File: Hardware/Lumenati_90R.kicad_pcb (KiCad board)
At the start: 2 copper layers, 25.4 x 25.4 mm, 19 parts, among them J1 CONN_041X04_NO_SILK, J2 CONN_041X04_NO_SILK, U1 APA102, U2 APA102, U3 APA102

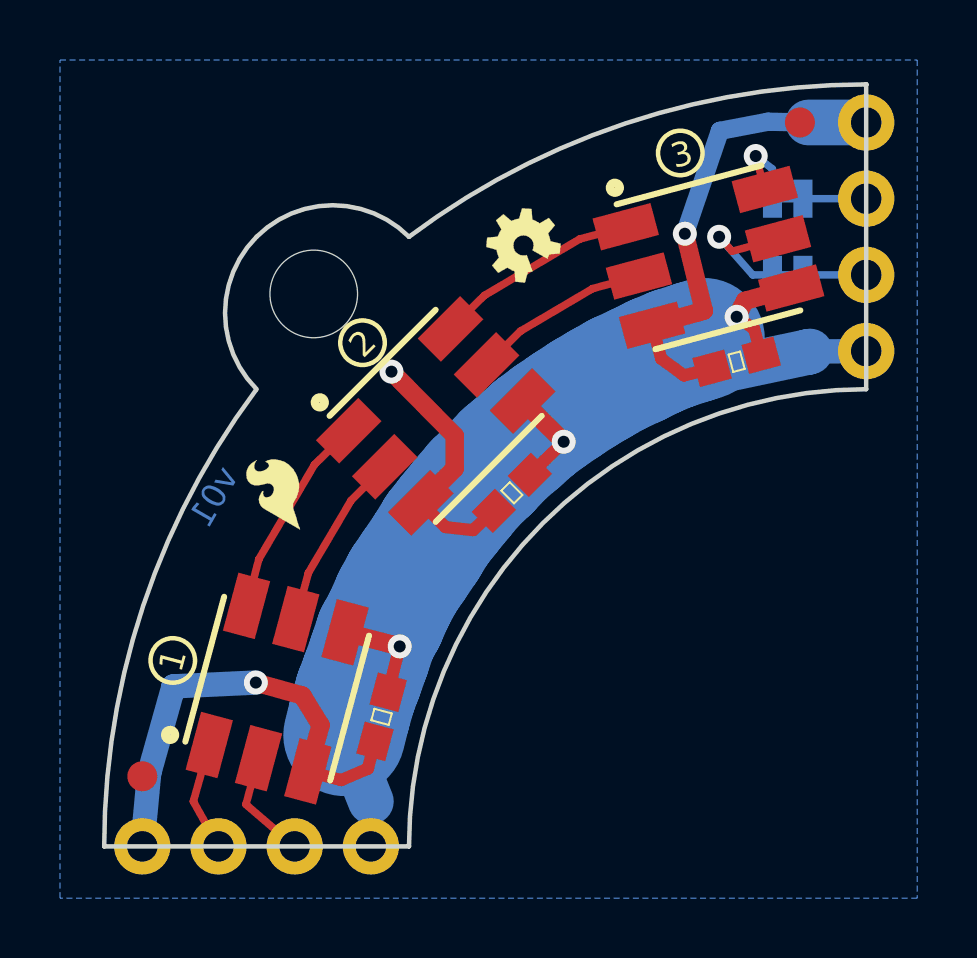
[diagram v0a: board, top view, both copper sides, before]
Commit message: Changed all the names to Lumenati, updated version to v10.
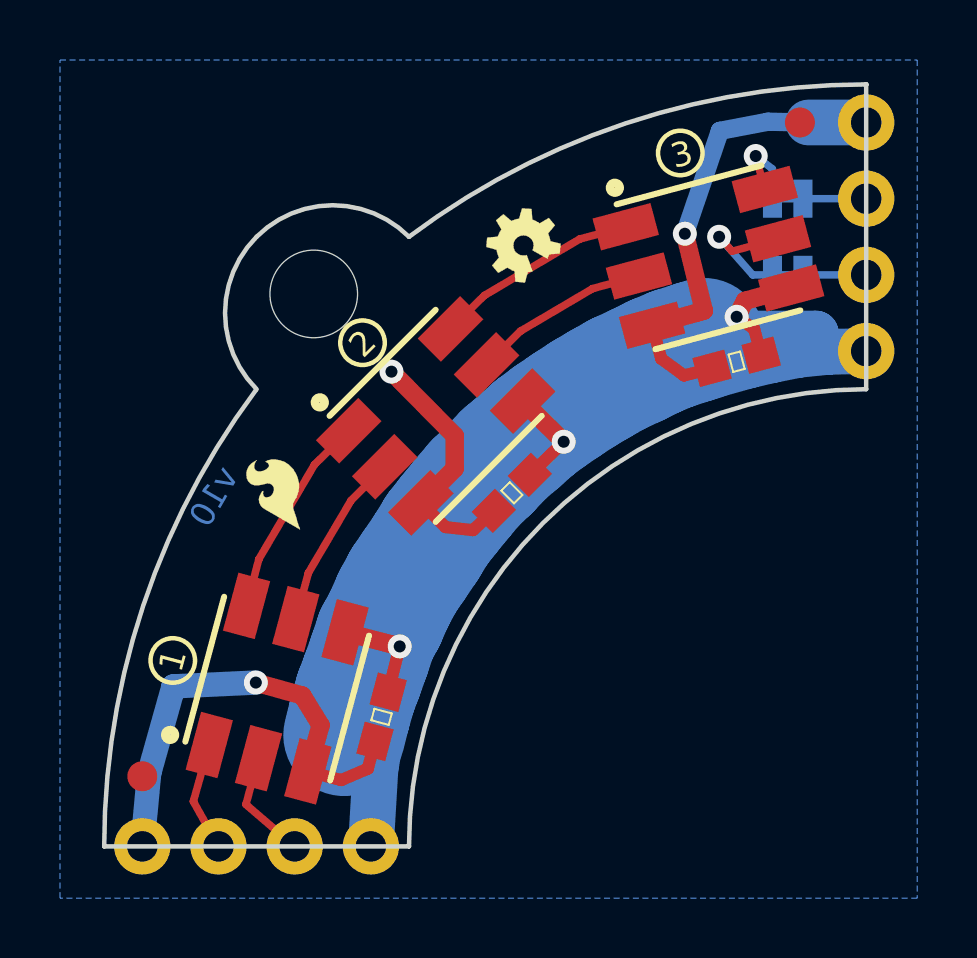
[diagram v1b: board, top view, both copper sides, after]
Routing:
- net +5V: track 45.1 -> 52.0 mm
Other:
- board text added: "Lumenati 90R"
- board text added: "v10"
- board text removed: "HiBeams 90R"
- board text removed: "v01"
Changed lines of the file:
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@@
     (thickness 1.6)
     (drawings 34)
-    (tracks 105)
+    (tracks 112)
     (zones 0)
     (modules 19)
@@
     (35 F.Paste user)
     (36 B.SilkS user)
-    (37 F.SilkS user)
+    (37 F.SilkS user hide)
     (38 B.Mask user)
     (39 F.Mask user)
-    (40 Dwgs.User user)
+    (40 Dwgs.User user hide)
     (41 Cmts.User user)
     (42 Eco1.User user)
@@
     (user_trace_width 0.8128)
     (user_trace_width 1.524)
-    (user_trace_width 3.175)
+    (user_trace_width 2.032)
     (user_trace_width 4.064)
     (trace_clearance 0.2)
@@
     (arrow2b (pts (xy 160.2232 121.539) (xy 159.096696 122.125421)))
   )
-  (gr_text v01 (at 271.0434 193.1924) (layer Cmts.User)
+  (gr_text v10 (at 271.0434 193.1924) (layer Cmts.User)
     (effects (font (size 1.5 1.5) (thickness 0.3)))
   )
@@
     (effects (font (size 1.5 1.5) (thickness 0.3)))
   )
-  (gr_text "HiBeams 90R" (at 194.5132 189.6364) (layer Cmts.User)
+  (gr_text "Lumenati 90R" (at 194.5132 189.6364) (layer Cmts.User)
     (effects (font (size 1.5 1.5) (thickness 0.3)))
   )
@@
     (effects (font (size 0.8128 0.8128) (thickness 0.1778)))
   )
-  (gr_text v01 (at 138.4808 104.7242 60) (layer B.Cu)
+  (gr_text v10 (at 138.4808 104.7242 60) (layer B.Cu)
     (effects (font (size 0.8128 0.8128) (thickness 0.1778)) (justify mirror))
   )
-  (gr_text "HiBeams 90R" (at 147.4216 103.5558 45) (layer B.SilkS)
+  (gr_text "Lumenati 90R" (at 147.4216 103.5558 45) (layer B.SilkS)
     (effects (font (size 1.5 1.5) (thickness 0.3)) (justify mirror))
   )
@@
   (segment (start 142.7226 114.173) (end 143.6116 113.792) (width 0.4064) (layer F.Cu) (net 1))
   (segment (start 143.6116 113.792) (end 143.849228 112.884253) (width 0.4064) (layer F.Cu) (net 1))
-  (segment (start 143.7132 114.8842) (end 142.8242 112.6744) (width 1.524) (layer B.Cu) (net 2))
-  (segment (start 143.7132 116.3828) (end 143.7132 114.8334) (width 0.8128) (layer B.Cu) (net 2))
-  (segment (start 143.7132 114.8334) (end 143.7132 114.8842) (width 0.8128) (layer B.Cu) (net 2))
+  (segment (start 158.5976 99.905312) (end 158.5468 99.2886) (width 1.524) (layer B.Cu) (net 2))
+  (segment (start 158.5468 99.2886) (end 155.3972 99.2886) (width 1.524) (layer B.Cu) (net 2))
+  (segment (start 155.3972 99.2886) (end 155.3972 99.029157) (width 1.524) (layer B.Cu) (net 2))
+  (segment (start 160.2232 99.8728) (end 158.5976 99.905312) (width 1.524) (layer B.Cu) (net 2))
+  (segment (start 158.5976 99.905312) (end 158.9532 99.8982) (width 1.524) (layer B.Cu) (net 2))
+  (segment (start 158.9532 99.8982) (end 157.9626 99.9998) (width 1.524) (layer B.Cu) (net 2))
+  (segment (start 157.9626 99.9998) (end 157.0736 100.1776) (width 1.524) (layer B.Cu) (net 2))
+  (segment (start 157.0736 100.1776) (end 156.3116 100.3554) (width 1.524) (layer B.Cu) (net 2))
+  (segment (start 156.3116 100.3554) (end 155.0416 100.711) (width 1.524) (layer B.Cu) (net 2))
+  (segment (start 155.0416 100.711) (end 154.4828 99.568) (width 1.524) (layer B.Cu) (net 2))
+  (segment (start 143.7132 116.3828) (end 143.8656 113.792) (width 1.524) (layer B.Cu) (net 2))
+  (segment (start 143.8656 113.792) (end 143.9926 113.0808) (width 1.524) (layer B.Cu) (net 2))
+  (segment (start 143.9926 113.0808) (end 143.002 111.9632) (width 1.524) (layer B.Cu) (net 2))
   (segment (start 156.724653 100.008828) (end 156.4894 99.1362) (width 0.4064) (layer F.Cu) (net 2))
   (segment (start 156.4894 99.1362) (end 155.9052 98.7298) (width 0.4064) (layer F.Cu) (net 2))
@@
   (segment (start 156.1846 98.1964) (end 155.9052 98.7298) (width 0.6096) (layer F.Cu) (net 2))
   (via (at 155.9052 98.7298) (size 0.8) (drill 0.4) (layers F.Cu B.Cu) (net 2))
-  (segment (start 155.9052 98.7298) (end 154.4828 99.568) (width 0.6096) (layer B.Cu) (net 2))
+  (segment (start 155.9052 98.7298) (end 155.3972 99.029157) (width 0.6096) (layer B.Cu) (net 2))
+  (segment (start 155.3972 99.029157) (end 154.4828 99.568) (width 0.6096) (layer B.Cu) (net 2))
   (segment (start 142.8242 112.6744) (end 143.002 111.9632) (width 4.064) (layer B.Cu) (net 2))
   (segment (start 143.002 111.9632) (end 143.2052 111.252) (width 4.064) (layer B.Cu) (net 2))
@@
   (segment (start 153.7716 99.7966) (end 154.4828 99.568) (width 4.064) (layer B.Cu) (net 2))
   (segment (start 154.4828 99.568) (end 154.813 99.4664) (width 4.064) (layer B.Cu) (net 2))
-  (segment (start 158.2166 99.6442) (end 158.271625 99.904843) (width 0.6096) (layer B.Cu) (net 2))
   (segment (start 149.012081 103.997319) (end 150.1394 102.8954) (width 0.4064) (layer F.Cu) (net 2))
   (segment (start 148.771338 101.536825) (end 150.1394 102.8954) (width 0.6096) (layer F.Cu) (net 2))
@@
   (via (at 144.67332 109.71784) (size 0.8) (drill 0.4) (layers F.Cu B.Cu) (net 2))
   (segment (start 144.67332 109.71784) (end 143.4084 110.7186) (width 0.6096) (layer B.Cu) (net 2))
-  (segment (start 158.35122 99.88804) (end 158.271625 99.904843) (width 1.524) (layer B.Cu) (net 2))
-  (segment (start 158.271625 99.904843) (end 155.37942 100.51542) (width 1.524) (layer B.Cu) (net 2))
   (segment (start 155.37942 100.51542) (end 154.813 99.4664) (width 1.524) (layer B.Cu) (net 2))
-  (segment (start 160.2232 99.8728) (end 158.35122 99.88804) (width 0.8128) (layer B.Cu) (net 2))
   (segment (start 138.6332 116.3828) (end 137.795 114.8842) (width 0.254) (layer F.Cu) (net 3))
   (segment (start 137.795 114.8842) (end 138.32576 113.00323) (width 0.254) (layer F.Cu) (net 3))
